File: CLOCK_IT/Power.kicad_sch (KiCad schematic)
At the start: 23 parts, among them SW1 CK_KMS2xxG, U4 AXP2101

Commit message: :tada: added USB
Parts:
- added U5: MC-264, easyeda2kicad:USB-C-SMD_MC-264, symbol MC-264:MC-264
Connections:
- net GND: now also U5.A1 (GND), U5.A12 (GND), U5.B1 (GND), U5.B12 (GND)
- new net +5V_USB: U5.A4 (VBUS), U5.A9 (VBUS), U5.B4 (VBUS), U5.B9 (VBUS)
- new net USB_DN: U5.A7 (DN1), U5.B7 (DN2)
- new net USB_DP: U5.A6 (DP1), U5.B6 (DP2)
- no-connect marks 7 -> 11

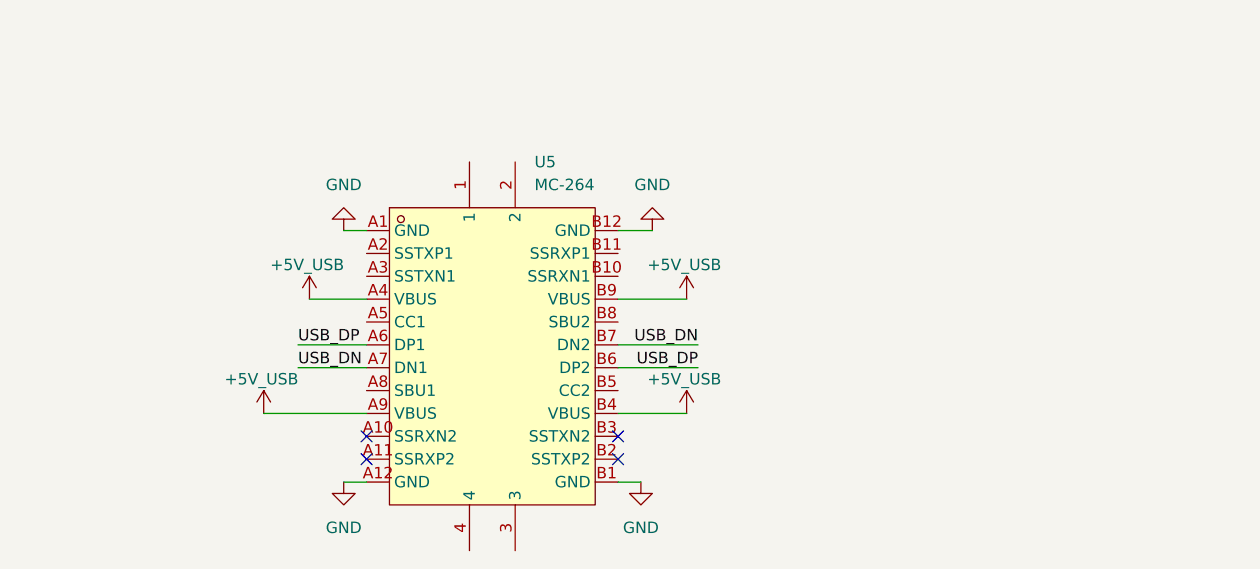
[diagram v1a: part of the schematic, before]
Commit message: :tada: completing usb design
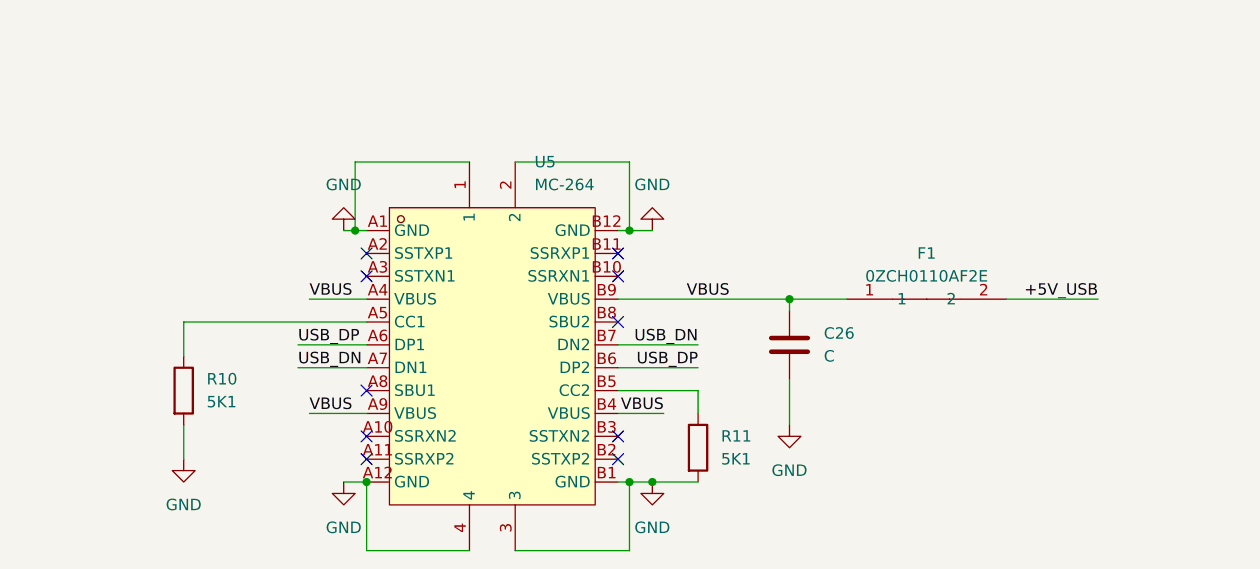
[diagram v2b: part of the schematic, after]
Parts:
- added C26: C, symbol Device:C
- added F1: 0ZCH0110AF2E, easyeda2kicad:F1210, symbol 0ZCH0110AF2E:0ZCH0110AF2E
- added R10, R11: 5K1, symbol Device:R
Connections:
- net +5V_USB: now also F1.2; no longer U5.A4 (VBUS), U5.A9 (VBUS), U5.B4 (VBUS), U5.B9 (VBUS)
- net GND: now also U5.1, U5.2, U5.3, U5.4, C26.2, R10.2, R11.2
- net at U5.A5 (CC1): now also R10.1
- net at U5.B5 (CC2): now also R11.1
- new net VBUS: C26.1, F1.1, U5.A4 (VBUS), U5.A9 (VBUS), U5.B4 (VBUS), U5.B9 (VBUS)
- no-connect marks 11 -> 17

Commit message: :fire: correcting PowerAXP section
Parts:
- removed D1: LED, symbol Device:LED
- added C28: 1uF, symbol Device:C
- added C33: 10uF/10V, symbol Device:C
- added C34: 22uF/10V, symbol Device:C
- added LED1: XL-0201SURC, easyeda2kicad:LED-SMD_L0.65-W0.35-P0.41_XL-0201SURC, symbol XL-0201SURC:XL-0201SURC
- C26: value C -> 0.1u
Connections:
- net +5V_USB is gone; now on net 5VSYS: F1.2
- net 4.4V_VBAT: now also C28.1
- net 5VSYS: now also LED1.1 (A)
- net GND: now also C28.2, C33.1, C34.1
- net VSYS: now also U4.34 (VSYS), C33.2, C34.2
- net at R6.1: now also LED1.2 (K)
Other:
- moved on the sheet: R7, R8, R9
